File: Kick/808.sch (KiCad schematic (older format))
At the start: 55 parts

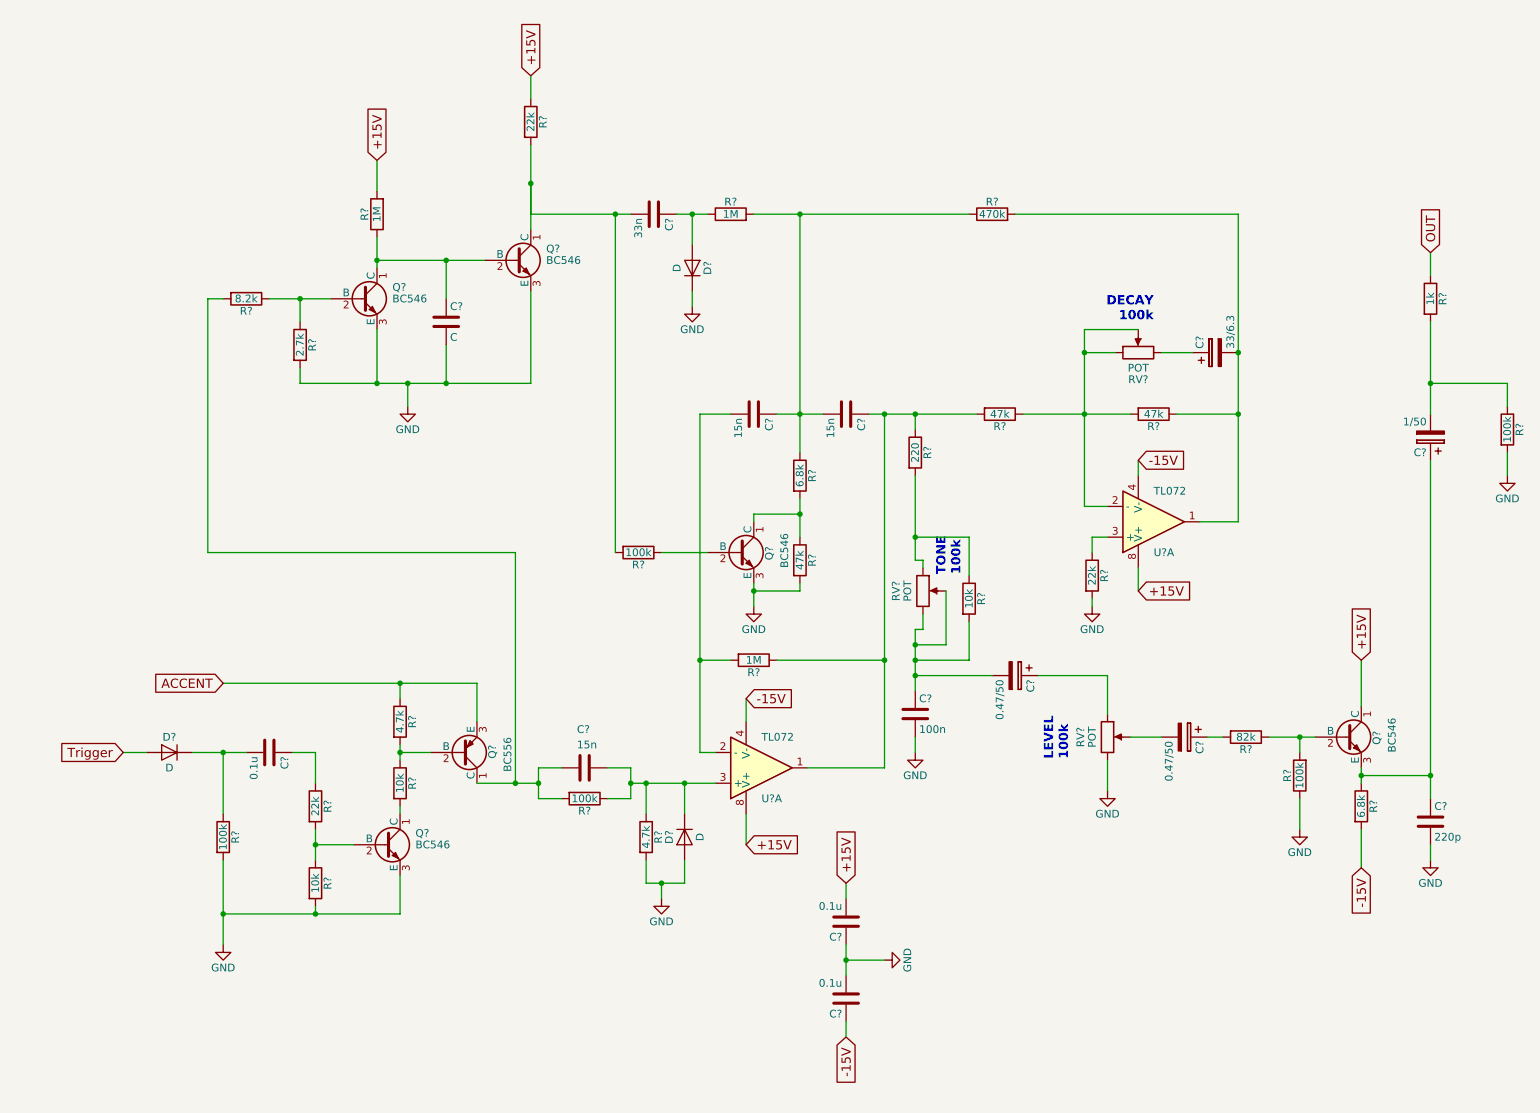
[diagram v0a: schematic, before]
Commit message: added pwr flags to snare
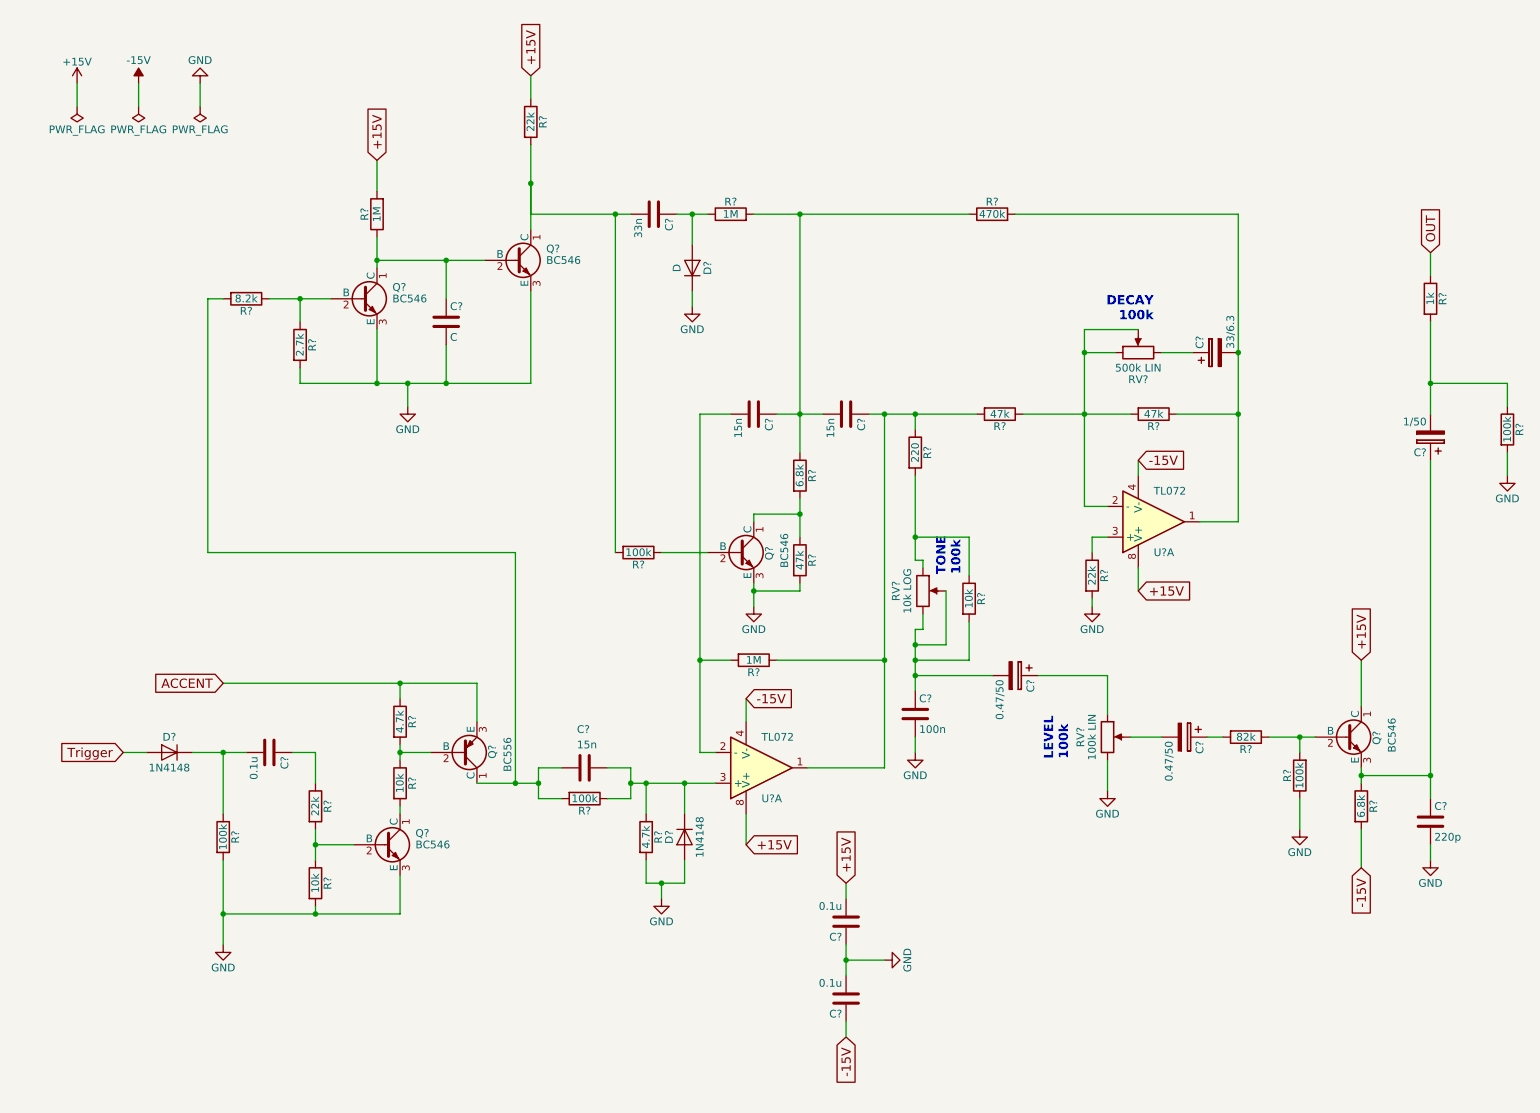
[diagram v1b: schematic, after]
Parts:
- D? (x2): value D -> 1N4148
- RV?: value POT -> 10k LOG
- RV?: value POT -> 500k LIN
- RV?: value POT -> 100k LIN
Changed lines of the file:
@@
 P 1500 5400
 F 0 "D?" H 1500 5500 50  0000 C CNN
-F 1 "D" H 1500 5300 50  0000 C CNN
+F 1 "1N4148" H 1500 5300 50  0000 C CNN
 F 2 "" H 1500 5400 50  0001 C CNN
 F 3 "" H 1500 5400 50  0001 C CNN
@@
 P 4850 5950
 F 0 "D?" H 4850 6050 50  0000 C CNN
-F 1 "D" H 4850 5850 50  0000 C CNN
+F 1 "1N4148" H 4850 5850 50  0000 C CNN
 F 2 "" H 4850 5950 50  0001 C CNN
 F 3 "" H 4850 5950 50  0001 C CNN
@@
 P 6400 4350
 F 0 "RV?" V 6225 4350 50  0000 C CNN
-F 1 "POT" V 6300 4350 50  0000 C CNN
+F 1 "10k LOG" V 6300 4350 50  0000 C CNN
 F 2 "" H 6400 4350 50  0001 C CNN
 F 3 "" H 6400 4350 50  0001 C CNN
@@
 P 7800 2800
 F 0 "RV?" V 7625 2800 50  0000 C CNN
-F 1 "POT" V 7700 2800 50  0000 C CNN
+F 1 "500k LIN" V 7700 2800 50  0000 C CNN
 F 2 "" H 7800 2800 50  0001 C CNN
 F 3 "" H 7800 2800 50  0001 C CNN
@@
 P 7600 5300
 F 0 "RV?" V 7425 5300 50  0000 C CNN
-F 1 "POT" V 7500 5300 50  0000 C CNN
+F 1 "100k LIN" V 7500 5300 50  0000 C CNN
 F 2 "" H 7600 5300 50  0001 C CNN
 F 3 "" H 7600 5300 50  0001 C CNN
@@
 Text Notes 7900 2600 2    60   ~ 12
 DECAY\n100k
+$Comp
+L PWR_FLAG #FLG?
+U 1 1 5AB8142B
+P 900 1200
+F 0 "#FLG?" H 900 1275 50  0001 C CNN
+F 1 "PWR_FLAG" H 900 1350 50  0000 C CNN
+F 2 "" H 900 1200 50  0001 C CNN
+F 3 "" H 900 1200 50  0001 C CNN
+	1    900  1200
+	-1   0    0    1
+$EndComp
+$Comp
+L PWR_FLAG #FLG?
+U 1 1 5AB814E2
+P 1300 1200
+F 0 "#FLG?" H 1300 1275 50  0001 C CNN
+F 1 "PWR_FLAG" H 1300 1350 50  0000 C CNN
+F 2 "" H 1300 1200 50  0001 C CNN
+F 3 "" H 1300 1200 50  0001 C CNN
+	1    1300 1200
+	-1   0    0    1
+$EndComp
+$Comp
+L PWR_FLAG #FLG?
+U 1 1 5AB81592
+P 1700 1200
+F 0 "#FLG?" H 1700 1275 50  0001 C CNN
+F 1 "PWR_FLAG" H 1700 1350 50  0000 C CNN
+F 2 "" H 1700 1200 50  0001 C CNN
+F 3 "" H 1700 1200 50  0001 C CNN
+	1    1700 1200
+	-1   0    0    1
+$EndComp
+$Comp
+L +15V #PWR?
+U 1 1 5AB81290
+P 900 1050
+F 0 "#PWR?" H 900 900 50  0001 C CNN
+F 1 "+15V" H 900 1190 50  0000 C CNN
+F 2 "" H 900 1050 50  0001 C CNN
+F 3 "" H 900 1050 50  0001 C CNN
+	1    900  1050
+	1    0    0    -1
+$EndComp
+$Comp
+L -15V #PWR?
+U 1 1 5AB81312
+P 1300 1050
+F 0 "#PWR?" H 1300 1150 50  0001 C CNN
+F 1 "-15V" H 1300 1200 50  0000 C CNN
+F 2 "" H 1300 1050 50  0001 C CNN
+F 3 "" H 1300 1050 50  0001 C CNN
+	1    1300 1050
+	1    0    0    -1
+$EndComp
+$Comp
+L GND #PWR?
+U 1 1 5AB813C9
+P 1700 1050
+F 0 "#PWR?" H 1700 800 50  0001 C CNN
+F 1 "GND" H 1700 900 50  0000 C CNN
+F 2 "" H 1700 1050 50  0001 C CNN
+F 3 "" H 1700 1050 50  0001 C CNN
+	1    1700 1050
+	-1   0    0    1
+$EndComp
+Wire Wire Line
+	1700 1050 1700 1200
+Wire Wire Line
+	1300 1050 1300 1200
+Wire Wire Line
+	900  1050 900  1200
 $EndSCHEMATC

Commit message: kick almost done
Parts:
- removed U?: TL072, symbol TL072
- added J1: Trigger In, Pin_Headers:Pin_Header_Straight_1x02_Pitch2.00mm, symbol CONN_01X02
- added J2: Trigger OUT, Pin_Headers:Pin_Header_Straight_1x02_Pitch2.00mm, symbol CONN_01X02
- added SW1: Trigger, Buttons_Switches_THT:SW_PUSH_6mm, symbol SW_Push
- added unit 2 of U1
- C1, C7, C8, C9: renamed from C?; footprint (none) -> Capacitors_THT:C_Disc_D3.0mm_W1.6mm_P2.50mm
- C10, C11, C13: renamed from C?; footprint (none) -> Capacitors_THT:CP_Radial_D4.0mm_P2.00mm
- C12: renamed from C?; footprint (none) -> Capacitors_THT:CP_Radial_D5.0mm_P2.00mm
- C14, C3, C4, C5, C6: renamed from C?; footprint (none) -> Capacitors_THT:C_Disc_D7.0mm_W2.5mm_P5.00mm
- C2: renamed from C?; value C -> 100n; footprint (none) -> Capacitors_THT:C_Disc_D3.0mm_W1.6mm_P2.50mm
- D1: renamed from D?; value 1N4148 -> 1N914A; footprint (none) -> Diodes_THT:D_A-405_P7.62mm_Horizontal
- D2: renamed from D?; footprint (none) -> Diodes_THT:D_A-405_P7.62mm_Horizontal
- D3: renamed from D?; value D -> 1N4148; footprint (none) -> Diodes_THT:D_A-405_P7.62mm_Horizontal
- R1, R10, R11, R12, R13, R14, R15, R16, R17, R18, R19, R2, R20, R21, R22, R23, R24, R25, R26, R27, R3, R4, R5, R6, R7, R8, R9: renamed from R?; footprint (none) -> Resistors_THT:R_Axial_DIN0204_L3.6mm_D1.6mm_P5.08mm_Horizontal
- RV1, RV2, RV3: renamed from RV?; footprint (none) -> Pin_Headers:Pin_Header_Straight_1x03_Pitch2.00mm
- U1: renamed from U?; footprint (none) -> Housings_DIP:DIP-8_W7.62mm
- gave numbers to parts that had none: 6
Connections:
- net ACCENT is gone; now on net +15V: Q3.3 (E), R7.1
- net +15V: now also SW1.2, U1.8 (V+)
- net -15V: now also U1.4 (V-)
- net GND: now also J1.2 (P2), J2.2 (P2)
- net at R20.1, R22.2, RV3.1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: now also U1.6 (-)
- net at C12.2, R19.2, R22.1: now also U1.7
- net at R21.1: now also U1.5 (+)
- net OUT: no longer names the net of R26.1
- net OUT: now also J2.1 (P1)
- net Trigger: no longer names the net of D1.2 (A)
- net Trigger: now also J1.1 (P1), SW1.1
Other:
- note added: "ACCENT"
- note added: "tied to +15V for now. Could be used differently"

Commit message: kick done with higher track width
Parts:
- added J3: CONN, Connectors_Terminal_Blocks:TerminalBlock_bornier-3_P5.08mm, symbol CONN_01X03
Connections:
- net +15V: now also J3.1 (P1)
- net -15V: now also J3.3 (P3)
- net GND: now also J3.2 (P2)
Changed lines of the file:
@@
 $EndComp
 $Comp
-L GND #PWR5
+L GND #PWR01
 U 1 1 5AB66FC2
 P 1850 6650
-F 0 "#PWR5" H 1850 6400 50  0001 C CNN
+F 0 "#PWR01" H 1850 6400 50  0001 C CNN
 F 1 "GND" H 1850 6500 50  0000 C CNN
 F 2 "" H 1850 6650 50  0001 C CNN
@@
 $EndComp
 $Comp
-L GND #PWR7
+L GND #PWR02
 U 1 1 5AB685F2
 P 4700 6350
-F 0 "#PWR7" H 4700 6100 50  0001 C CNN
+F 0 "#PWR02" H 4700 6100 50  0001 C CNN
 F 1 "GND" H 4700 6200 50  0000 C CNN
 F 2 "" H 4700 6350 50  0001 C CNN
@@
 $EndComp
 $Comp
-L GND #PWR6
+L GND #PWR03
 U 1 1 5AB68EA3
 P 3050 3150
-F 0 "#PWR6" H 3050 2900 50  0001 C CNN
+F 0 "#PWR03" H 3050 2900 50  0001 C CNN
 F 1 "GND" H 3050 3000 50  0000 C CNN
 F 2 "" H 3050 3150 50  0001 C CNN
@@
 $EndComp
 $Comp
-L GND #PWR9
+L GND #PWR04
 U 1 1 5AB69E18
 P 5300 4450
-F 0 "#PWR9" H 5300 4200 50  0001 C CNN
+F 0 "#PWR04" H 5300 4200 50  0001 C CNN
 F 1 "GND" H 5300 4300 50  0000 C CNN
 F 2 "" H 5300 4450 50  0001 C CNN
@@
 $EndComp
 $Comp
-L GND #PWR8
+L GND #PWR05
 U 1 1 5AB6AE86
 P 4900 2500
-F 0 "#PWR8" H 4900 2250 50  0001 C CNN
+F 0 "#PWR05" H 4900 2250 50  0001 C CNN
 F 1 "GND" H 4900 2350 50  0000 C CNN
 F 2 "" H 4900 2500 50  0001 C CNN
@@
 $EndComp
 $Comp
-L GND #PWR11
+L GND #PWR06
 U 1 1 5AB6C184
 P 6350 5400
-F 0 "#PWR11" H 6350 5150 50  0001 C CNN
+F 0 "#PWR06" H 6350 5150 50  0001 C CNN
 F 1 "GND" H 6350 5250 50  0000 C CNN
 F 2 "" H 6350 5400 50  0001 C CNN
@@
 $EndComp
 $Comp
-L GND #PWR14
+L GND #PWR07
 U 1 1 5AB6CA4A
 P 8850 5900
-F 0 "#PWR14" H 8850 5650 50  0001 C CNN
+F 0 "#PWR07" H 8850 5650 50  0001 C CNN
 F 1 "GND" H 8850 5750 50  0000 C CNN
 F 2 "" H 8850 5900 50  0001 C CNN
@@
 $EndComp
 $Comp
-L GND #PWR15
+L GND #PWR08
 U 1 1 5AB6DAB4
 P 9700 6100
-F 0 "#PWR15" H 9700 5850 50  0001 C CNN
+F 0 "#PWR08" H 9700 5850 50  0001 C CNN
 F 1 "GND" H 9700 5950 50  0000 C CNN
 F 2 "" H 9700 6100 50  0001 C CNN
@@
 $EndComp
 $Comp
-L GND #PWR17
+L GND #PWR09
 U 1 1 5AB6E3B6
 P 10200 3600
-F 0 "#PWR17" H 10200 3350 50  0001 C CNN
+F 0 "#PWR09" H 10200 3350 50  0001 C CNN
 F 1 "GND" H 10200 3450 50  0000 C CNN
 F 2 "" H 10200 3600 50  0001 C CNN
@@
 $EndComp
 $Comp
-L GND #PWR13
+L GND #PWR010
 U 1 1 5AB6EF83
 P 7600 5650
-F 0 "#PWR13" H 7600 5400 50  0001 C CNN
+F 0 "#PWR010" H 7600 5400 50  0001 C CNN
 F 1 "GND" H 7600 5500 50  0000 C CNN
 F 2 "" H 7600 5650 50  0001 C CNN
@@
 $EndComp
 $Comp
-L GND #PWR12
+L GND #PWR011
 U 1 1 5AB6F652
 P 7500 4450
-F 0 "#PWR12" H 7500 4200 50  0001 C CNN
+F 0 "#PWR011" H 7500 4200 50  0001 C CNN
 F 1 "GND" H 7500 4300 50  0000 C CNN
 F 2 "" H 7500 4450 50  0001 C CNN
@@
 	6700 4550 6700 4800
 Wire Wire Line
-	6350 4800 6700 4800
+	6700 4800 6350 4800
 Wire Wire Line
 	6350 4600 6350 5000
@@
 $EndComp
 $Comp
-L GND #PWR10
+L GND #PWR012
 U 1 1 5AB71B07
 P 6150 6750
-F 0 "#PWR10" H 6150 6500 50  0001 C CNN
+F 0 "#PWR012" H 6150 6500 50  0001 C CNN
 F 1 "GND" H 6150 6600 50  0000 C CNN
 F 2 "" H 6150 6750 50  0001 C CNN
@@
 DECAY\n100k
 $Comp
-L PWR_FLAG #FLG1
+L PWR_FLAG #FLG013
 U 1 1 5AB8142B
 P 900 1200
-F 0 "#FLG1" H 900 1275 50  0001 C CNN
+F 0 "#FLG013" H 900 1275 50  0001 C CNN
 F 1 "PWR_FLAG" H 900 1350 50  0000 C CNN
 F 2 "" H 900 1200 50  0001 C CNN
@@
 $EndComp
 $Comp
-L PWR_FLAG #FLG2
+L PWR_FLAG #FLG014
 U 1 1 5AB814E2
 P 1300 1200
-F 0 "#FLG2" H 1300 1275 50  0001 C CNN
+F 0 "#FLG014" H 1300 1275 50  0001 C CNN
 F 1 "PWR_FLAG" H 1300 1350 50  0000 C CNN
 F 2 "" H 1300 1200 50  0001 C CNN
@@
 $EndComp
 $Comp
-L PWR_FLAG #FLG3
+L PWR_FLAG #FLG015
 U 1 1 5AB81592
 P 1700 1200
-F 0 "#FLG3" H 1700 1275 50  0001 C CNN
+F 0 "#FLG015" H 1700 1275 50  0001 C CNN
 F 1 "PWR_FLAG" H 1700 1350 50  0000 C CNN
 F 2 "" H 1700 1200 50  0001 C CNN
@@
 $EndComp
 $Comp
-L +15V #PWR1
+L +15V #PWR016
 U 1 1 5AB81290
 P 900 1050
-F 0 "#PWR1" H 900 900 50  0001 C CNN
+F 0 "#PWR016" H 900 900 50  0001 C CNN
 F 1 "+15V" H 900 1190 50  0000 C CNN
 F 2 "" H 900 1050 50  0001 C CNN
@@
 $EndComp
 $Comp
-L GND #PWR4
+L GND #PWR017
 U 1 1 5AB813C9
 P 1700 1050
-F 0 "#PWR4" H 1700 800 50  0001 C CNN
+F 0 "#PWR017" H 1700 800 50  0001 C CNN
 F 1 "GND" H 1700 900 50  0000 C CNN
 F 2 "" H 1700 1050 50  0001 C CNN
@@
 $EndComp
 $Comp
-L GND #PWR3
+L GND #PWR018
 U 1 1 5AB8F345
 P 1300 5600
-F 0 "#PWR3" H 1300 5350 50  0001 C CNN
+F 0 "#PWR018" H 1300 5350 50  0001 C CNN
 F 1 "GND" H 1300 5450 50  0000 C CNN
 F 2 "" H 1300 5600 50  0001 C CNN
@@
 $EndComp
 $Comp
-L GND #PWR16
+L GND #PWR019
 U 1 1 5AB9060E
 P 10000 2250
-F 0 "#PWR16" H 10000 2000 50  0001 C CNN
+F 0 "#PWR019" H 10000 2000 50  0001 C CNN
 F 1 "GND" H 10000 2100 50  0000 C CNN
 F 2 "" H 10000 2250 50  0001 C CNN
@@
 Wire Wire Line
 	1100 4350 1100 4550
+Connection ~ 900  1150
+Wire Wire Line
+	1150 1150 1300 1150
+Connection ~ 1300 1150
+Wire Wire Line
+	1500 1150 1700 1150
+Connection ~ 1700 1150
+$Comp
+L +15V #PWR020
+U 1 1 5ABD3895
+P 2550 1600
+F 0 "#PWR020" H 2550 1450 50  0001 C CNN
+F 1 "+15V" H 2550 1740 50  0000 C CNN
+F 2 "" H 2550 1600 50  0001 C CNN
+F 3 "" H 2550 1600 50  0001 C CNN
+	1    2550 1600
+	1    0    0    -1
+$EndComp
+$Comp
+L -15V #PWR11
+U 1 1 5ABD3957
+P 5750 5150
+F 0 "#PWR11" H 5750 5250 50  0001 C CNN
+F 1 "-15V" H 5750 5300 50  0000 C CNN
+F 2 "" H 5750 5150 50  0001 C CNN
+F 3 "" H 5750 5150 50  0001 C CNN
+	1    5750 5150
+	1    0    0    -1
+$EndComp
+Wire Wire Line
+	2550 1600 2550 1700
+Wire Wire Line
+	2550 1700 2850 1700
+Connection ~ 2850 1700
+Wire Wire Line
+	5750 5150 5250 5150
+Connection ~ 5250 5150
+$Comp
+L CONN_01X03 J3
+U 1 1 5ABD46C2
+P 600 2300
+F 0 "J3" H 600 2500 50  0000 C CNN
+F 1 "CONN" H 600 2050 50  0000 C CNN
+F 2 "Connectors_Terminal_Blocks:TerminalBlock_bornier-3_P5.08mm" H 600 2300 50  0001 C CNN
+F 3 "" H 600 2300 50  0001 C CNN
+	1    600  2300
+	-1   0    0    -1
+$EndComp
+Wire Wire Line
+	1500 1150 1500 2300
+Wire Wire Line
+	1150 1150 1150 2400
+Wire Wire Line
+	800  2200 800  1150
+Wire Wire Line
+	1500 2300 800  2300
+Wire Wire Line
+	1150 2400 800  2400
+Wire Wire Line
+	800  1150 900  1150
 $EndSCHEMATC
